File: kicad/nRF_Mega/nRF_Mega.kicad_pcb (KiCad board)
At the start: 2 copper layers, 85.1 x 53.3 mm, 11 parts, among them J1 Screw_Terminal_01x02, M1 Motor_Servo, M2 Motor_Servo, M3 Motor_Servo, M4 Motor_Servo, M5 Motor_Servo, U1 NRF24L01_Breakout

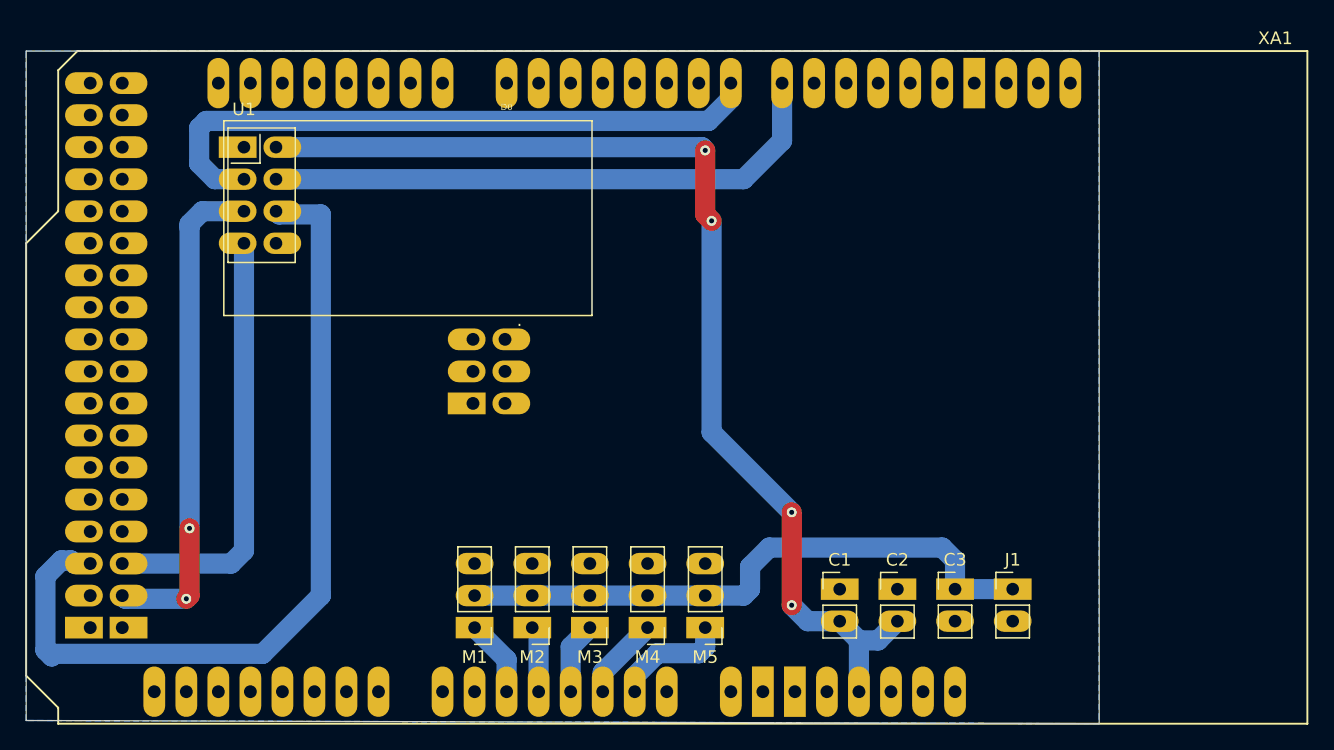
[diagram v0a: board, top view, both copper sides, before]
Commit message: corrected nRF placement, minimized wire length, fixed caps and connector
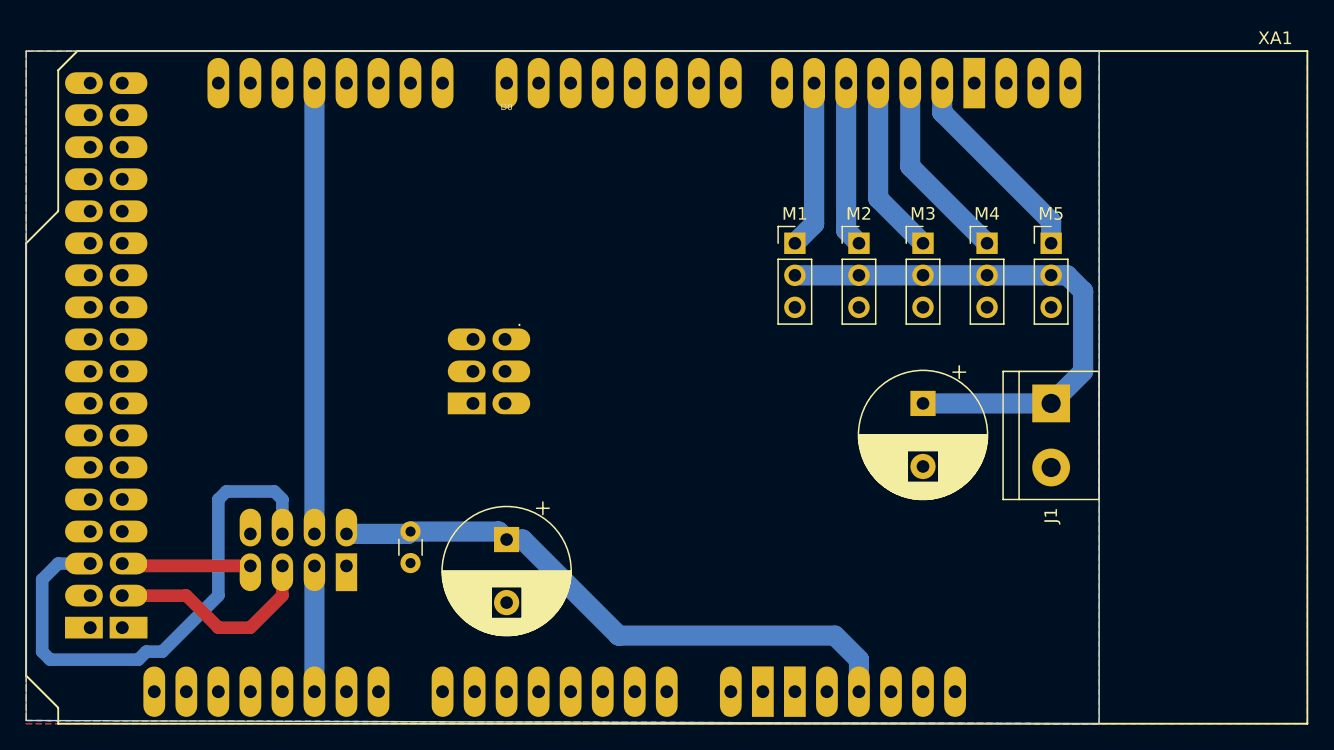
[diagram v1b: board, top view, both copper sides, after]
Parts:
- C1: value C -> .1 uF; footprint arduino-library:PinHeader_1x02_P2.54mm_Vertical -> Capacitor_THT:C_Disc_D3.0mm_W1.6mm_P2.50mm
- C2, C3: value C -> 470 uF; footprint arduino-library:PinHeader_1x02_P2.54mm_Vertical -> Capacitor_THT:CP_Radial_D10.0mm_P5.00mm
- J1: footprint arduino-library:PinHeader_1x02_P2.54mm_Vertical -> TerminalBlock:TerminalBlock_bornier-2_P5.08mm
- M1, M2, M3, M4, M5: footprint arduino-library:PinHeader_1x03_P2.54mm_Vertical_Custom -> Connector_PinHeader_2.54mm:PinHeader_1x03_P2.54mm_Vertical
- U1: moved to B.Cu
- moved M5 41.0 mm to (106.7, 33.0), turned to 0 degrees
- moved M4 40.7 mm to (101.6, 33.0), turned to 0 degrees
- moved M3 40.3 mm to (96.5, 33.0), turned to 0 degrees
- moved M2 40.0 mm to (91.4, 33.0), turned to 0 degrees
- moved M1 39.7 mm to (86.4, 33.0), turned to 0 degrees
- moved C1 34.3 mm to (55.9, 55.9), turned to -90 degrees
- moved U1 34.2 mm to (50.8, 58.6), turned to 90 degrees
- moved C2 31.2 mm to (63.5, 56.5), turned to -90 degrees
- moved J1 15.0 mm to (106.7, 45.7), turned to -90 degrees
- moved C3 14.9 mm to (96.5, 45.7), turned to -90 degrees
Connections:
- C1 pad 1: GND -> +3.3V
- C1 pad 2: Net-(U1-VCC) -> GND
- C2 pad 1: GND -> +3.3V
- C2 pad 2: Net-(U1-VCC) -> GND
- U1 pad 2: Net-(U1-VCC) -> +3.3V
- XA1 pad 3V3: Net-(U1-VCC) -> +3.3V
- XA1 pad A1: Net-(M5-PWM) -> unconnected-(XA1-PadA1)
- XA1 pad A10: unconnected-(XA1-PadA10) -> Net-(U1-CE)
- XA1 pad A2: Net-(M4-PWM) -> unconnected-(XA1-PadA2)
- XA1 pad A3: Net-(M3-PWM) -> unconnected-(XA1-PadA3)
- XA1 pad A4: Net-(M2-PWM) -> unconnected-(XA1-PadA4)
- XA1 pad A5: Net-(M1-PWM) -> unconnected-(XA1-PadA5)
- XA1 pad D10: unconnected-(XA1-PadD10) -> Net-(M2-PWM)
- XA1 pad D11: unconnected-(XA1-PadD11) -> Net-(M3-PWM)
- XA1 pad D12: unconnected-(XA1-PadD12) -> Net-(M4-PWM)
- XA1 pad D13: unconnected-(XA1-PadD13) -> Net-(M5-PWM)
- XA1 pad D18: unconnected-(XA1-D18/TX1-PadD18) -> Net-(U1-~{CSN})
- XA1 pad D7: Net-(U1-CE) -> unconnected-(XA1-PadD7)
- XA1 pad D8: Net-(U1-~{CSN}) -> unconnected-(XA1-PadD7)
- XA1 pad D9: unconnected-(XA1-PadD9) -> Net-(M1-PWM)
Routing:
- net Net-(U1-VCC): track 87.3 -> 0.00 mm, vias 4 -> 0
- net +3.3V: track 0.00 -> 47.5 mm
- net Net-(U1-CE): track 51.2 -> 9.97 mm
- net Net-(U1-MOSI): track 68.0 -> 42.3 mm
- net Net-(U1-MISO): track 34.5 -> 10.2 mm
- net Net-(U1-SCK): track 39.7 -> 17.2 mm, vias 2 -> 0
- net Net-(U1-~{CSN}): track 46.0 -> 35.7 mm
- net Net-(M4-PWM): track 6.55 -> 15.2 mm
- net Net-(M3-PWM): track 5.71 -> 14.2 mm
- net Net-(M2-PWM): track 5.29 -> 13.1 mm
- net Net-(M1-PWM): track 6.13 -> 13.3 mm
- net Net-(M5-PWM): track 9.31 -> 16.3 mm
- net Net-(J1-Pin_1): track 48.0 -> 43.5 mm
- added copper zone on B.Cu, net (none)
- added copper zone on B.Cu, net +3.3V
- added copper zone on F.Cu, net GND
- removed copper zone on B.Cu, net GND
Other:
- board text added: "+5V"
- board text added: "D10"
- board text added: "D11"
- board text added: "D12"
- board text added: "D13"
- board text added: "D9"
- board text added: "GND"
- board text added: "Signal"
